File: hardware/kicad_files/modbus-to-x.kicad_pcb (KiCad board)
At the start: 4 copper layers, 87.6 x 46.7 mm, 67 parts, among them IC1 ESP32-WROOM-32D_M113DH2800PH3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, J1 615006138421, J4 M50-3140545R, Q1 DSS4160U-7, Q2 DSS4160U-7, SW1 SW_Wuerth_450301014042, SW4 3983, U1 LM2596S-3.3, U3 MAX3485, Y1 32.768kHz

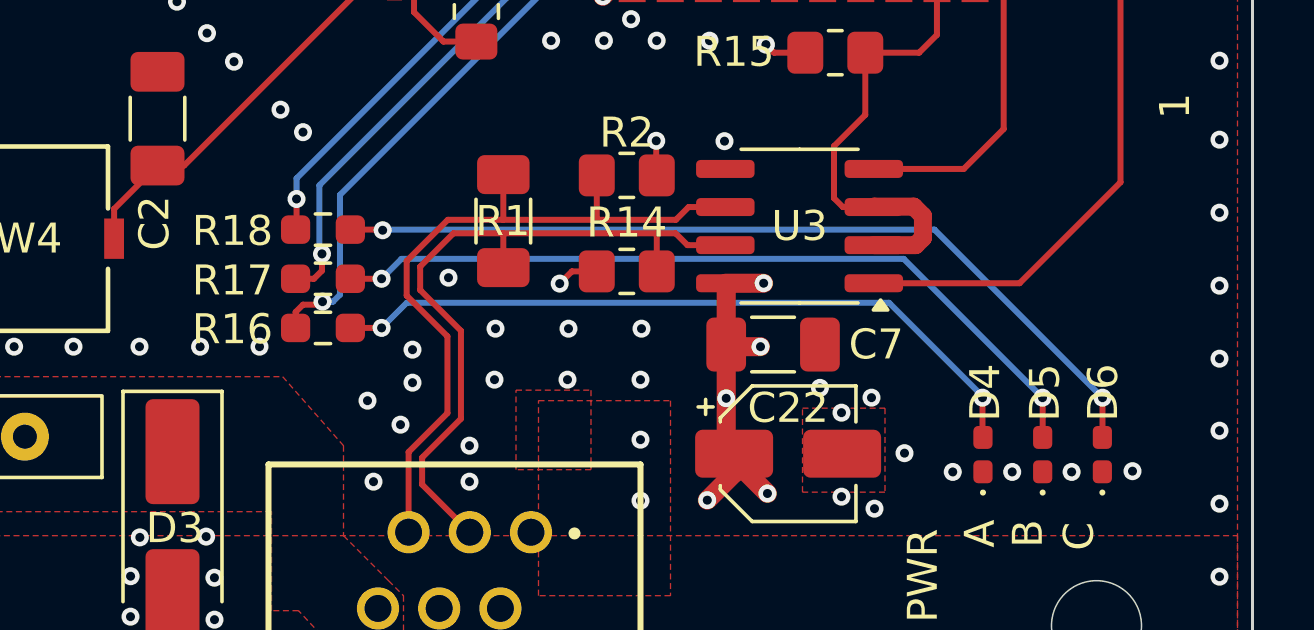
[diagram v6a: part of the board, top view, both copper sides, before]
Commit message: updated schema to reflect current configuration model
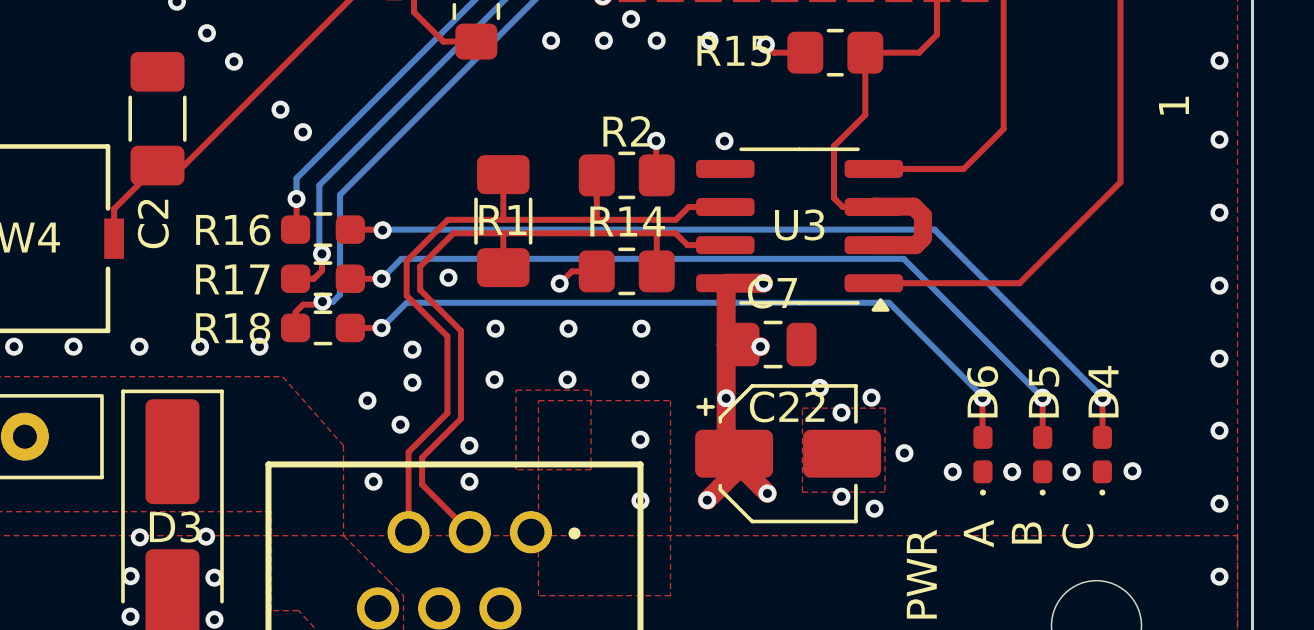
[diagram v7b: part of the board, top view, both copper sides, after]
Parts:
- C7: footprint Capacitor_SMD:C_1206_3216Metric_Pad1.33x1.80mm_HandSolder -> Capacitor_SMD:C_0805_2012Metric
- moved D4 3.98 mm to (127.5, 123.0)
- moved D6 3.98 mm to (123.5, 123.0)
- moved R16 3.28 mm to (101.5, 115.5)
- moved R18 3.28 mm to (101.5, 118.8)
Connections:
- R16 pad 1: /LED_A -> /LED_C
- R18 pad 1: /LED_C -> /LED_A
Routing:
- net Net-(D6-A): track 28.7 -> 24.1 mm
- net Net-(D4-A): track 24.1 -> 28.7 mm
